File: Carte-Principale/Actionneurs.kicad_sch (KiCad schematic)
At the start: 0 parts

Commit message: Moteurs + Encodeurs
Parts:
- added U7: PCA9685PW, Package_SO:TSSOP-28_4.4x9.7mm_P0.65mm, symbol Driver_LED:PCA9685PW
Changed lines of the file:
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@@
 	(generator_version "8.0")
 	(paper "A4")
+	(symbol
+		(lib_id "Driver_LED:PCA9685PW")
+		(at 151.13 81.28 0)
+		(unit 1)
+		(exclude_from_sim no)
+		(in_bom yes)
+		(on_board yes)
+		(dnp no)
+		(fields_autoplaced yes)
+		(property "Reference" "U7"
+			(at 153.3241 55.88 0)
+			(effects
+				(font
+					(size 1.27 1.27)
+				)
+				(justify left)
+			)
+		)
+		(property "Value" "PCA9685PW"
+			(at 153.3241 58.42 0)
+			(effects
+				(font
+					(size 1.27 1.27)
+				)
+				(justify left)
+			)
+		)
+		(property "Footprint" "Package_SO:TSSOP-28_4.4x9.7mm_P0.65mm"
+			(at 151.765 106.045 0)
+			(effects
+				(font
+					(size 1.27 1.27)
+				)
+				(justify left)
+				(hide yes)
+			)
+		)
+		(property "Datasheet" "http://www.nxp.com/docs/en/data-sheet/PCA9685.pdf"
+			(at 140.97 63.5 0)
+			(effects
+				(font
+					(size 1.27 1.27)
+				)
+				(hide yes)
+			)
+		)
+		(property "Description" "16-channel 12-bit PWM Fm+ I2C-bus LED controller RGBA TSSOP"
+			(at 151.13 81.28 0)
+			(effects
+				(font
+					(size 1.27 1.27)
+				)
+				(hide yes)
+			)
+		)
+		(pin "20"
+		)
+		(pin "28"
+		)
+		(pin "16"
+		)
+		(pin "10"
+		)
+		(pin "15"
+		)
+		(pin "9"
+		)
+		(pin "27"
+		)
+		(pin "12"
+		)
+		(pin "2"
+		)
+		(pin "21"
+		)
+		(pin "22"
+		)
+		(pin "8"
+		)
+		(pin "17"
+		)
+		(pin "11"
+		)
+		(pin "3"
+		)
+		(pin "24"
+		)
+		(pin "5"
+		)
+		(pin "25"
+		)
+		(pin "6"
+		)
+		(pin "1"
+		)
+		(pin "14"
+		)
+		(pin "7"
+		)
+		(pin "23"
+		)
+		(pin "4"
+		)
+		(pin "18"
+		)
+		(pin "13"
+		)
+		(pin "19"
+		)
+		(pin "26"
+		)
+		(instances
+			(project "Carte-Principale"
+				(path "/88b0dd29-ac24-4c5d-804c-fc642ecf6263/ec3b2e47-1720-4ba3-b32d-adf5bc711683"
+					(reference "U7")
+					(unit 1)
+				)
+			)
+		)
+	)
 )

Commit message: Avancée Actionneur
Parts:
- added C5: 10u, symbol Device:C
- added C6: x, symbol Device:C_Polarized
- added D1: RGB_LED, symbol Device:LED_BGKR
- added J5: AX12, symbol Connector:Conn_01x03_Pin
- added JP1: A0, symbol Jumper:SolderJumper_2_Open
- added JP2: A1, symbol Jumper:SolderJumper_2_Open
- added JP3: A2, symbol Jumper:SolderJumper_2_Open
- added JP4: A3, symbol Jumper:SolderJumper_2_Open
- added JP5: A4, symbol Jumper:SolderJumper_2_Open
- added JP6: A5, symbol Jumper:SolderJumper_2_Open
- added M1, M10, M11, M12, M13, M2, M3, M4, M5, M6, M7, M8, M9: Motor_Servo, Connector_PinHeader_2.54mm:PinHeader_1x03_P2.54mm_Vertical, symbol Motor:Motor_Servo
- added R10, R11, R6, R7, R8, R9: 10k, symbol Device:R
- added R12, R13, R14, R15, R16, R17, R18, R19, R20, R21, R22, R23, R24, R25, R26, R27: 220, symbol Device:R
- added R5: 10k, symbol Device:R_Small
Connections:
- net at U7.1 (A0): now also JP1.2 (B), R11.1
- net at U7.10 (LED4): now also R16.1
- net at U7.11 (LED5): now also R17.1
- net at U7.12 (LED6): now also R18.1
- net at U7.13 (LED7): now also R19.1
- net GND: now reaches U7.14 (VSS)
- net GND: now also U7.25 (EXTCLK), C5.1, C6.2, D1.3 (K), M1.3 (-), M10.3 (-), M11.3 (-), M12.3 (-), M13.3 (-), M2.3 (-), M3.3 (-), M4.3 (-), M5.3 (-), M6.3 (-), M7.3 (-), M8.3 (-), M9.3 (-), R10.2, R11.2, R5.2, R6.2, R7.2, R8.2, R9.2
- net at U7.15 (LED8): now also R20.1
- net at U7.16 (LED9): now also R21.1
- net at U7.17 (LED10): now also R22.1
- net at U7.18 (LED11): now also R23.1
- net at U7.19 (LED12): now also R24.1
- net at U7.2 (A1): now also JP2.2 (B), R10.1
- net at U7.20 (LED13): now also R25.1
- net at U7.21 (LED14): now also R26.1
- net at U7.22 (LED15): now also R27.1
- net at U7.23 (~{OE}): now also R5.1
- net at U7.24 (A5): now also JP6.2 (B), R6.1
- net SCL: now reaches U7.26 (SCL)
- net SDA: now reaches U7.27 (SDA)
- net +5V: now reaches U7.28 (VDD)
- net +5V: now also C5.2, JP1.1 (A), JP2.1 (A), JP3.1 (A), JP4.1 (A), JP5.1 (A), JP6.1 (A)
- net at U7.3 (A2): now also JP3.2 (B), R9.1
- net at U7.4 (A3): now also JP4.2 (B), R8.1
- net at U7.5 (A4): now also JP5.2 (B), R7.1
- net at U7.6 (LED0): now also R13.1
- net at U7.7 (LED1): now also R12.1
- net at U7.8 (LED2): now also R14.1
- net at U7.9 (LED3): now also R15.1
- new net +5VA: C6.1, M1.2 (+), M10.2 (+), M11.2 (+), M12.2 (+), M13.2 (+), M2.2 (+), M3.2 (+), M4.2 (+), M5.2 (+), M6.2 (+), M7.2 (+), M8.2 (+), M9.2 (+)
- new net PWM0: M1.1 (PWM), R13.2
- new net PWM1: M2.1 (PWM), R12.2
- new net PWM10: M11.1 (PWM), R22.2
- new net PWM11: M12.1 (PWM), R23.2
- new net PWM12: M13.1 (PWM), R24.2
- new net PWM13: D1.1 (BA), R25.2
- new net PWM14: D1.2 (GA), R26.2
- new net PWM15: D1.4 (RA), R27.2
- new net PWM2: M3.1 (PWM), R14.2
- new net PWM3: M4.1 (PWM), R15.2
- new net PWM4: M5.1 (PWM), R16.2
- new net PWM5: M6.1 (PWM), R17.2
- new net PWM6: M7.1 (PWM), R18.2
- new net PWM7: M8.1 (PWM), R19.2
- new net PWM8: M9.1 (PWM), R20.2
- new net PWM9: M10.1 (PWM), R21.2

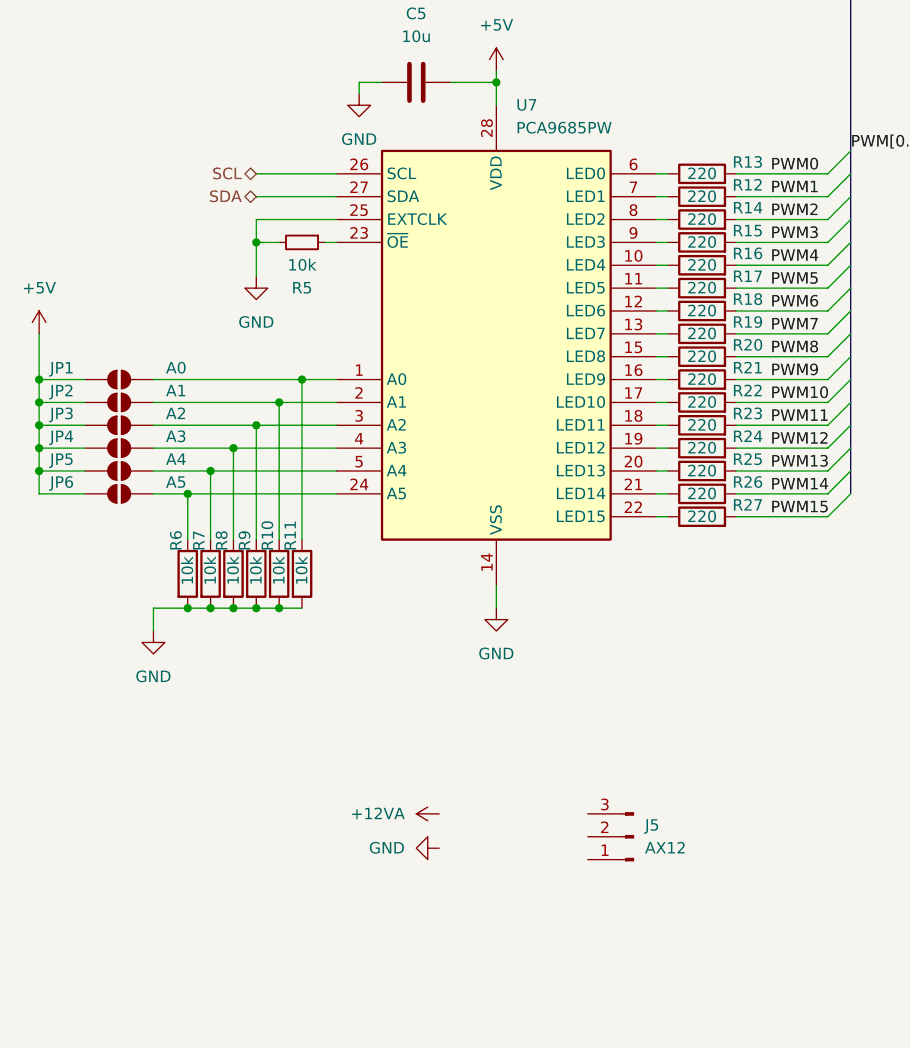
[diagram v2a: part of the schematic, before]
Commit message: Rajout écran
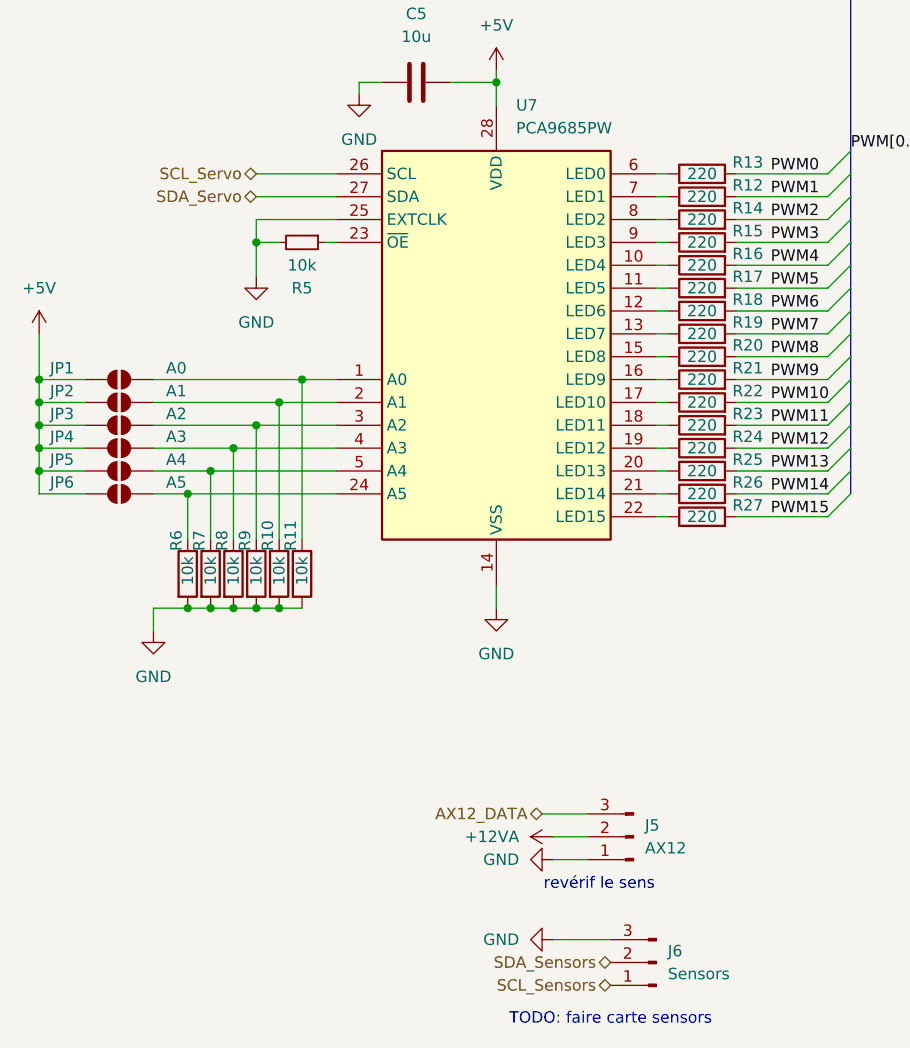
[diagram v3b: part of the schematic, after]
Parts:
- added J6: Sensors, symbol Connector:Conn_01x03_Pin
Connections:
- net +12VA: now also J5.2 (Pin_2)
- net GND: now also J5.1 (Pin_1), J6.3 (Pin_3)
- net AX12_DATA: now reaches J5.3 (Pin_3)
- net SCL renamed SCL_Servo
- net SDA renamed SDA_Servo
- new net SCL_Sensors: J6.1 (Pin_1)
- new net SDA_Sensors: J6.2 (Pin_2)
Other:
- note added: "TODO: faire carte sensors"
- note added: "revérif le sens"

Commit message: wiring
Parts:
- removed C5: 10u, symbol Device:C
- removed C6: x, symbol Device:C_Polarized
- removed D1: RGB_LED, symbol Device:LED_BGKR
- removed J6: Sensors, symbol Connector:Conn_01x03_Pin
- removed JP1: A0, symbol Jumper:SolderJumper_2_Open
- removed JP2: A1, symbol Jumper:SolderJumper_2_Open
- removed JP3: A2, symbol Jumper:SolderJumper_2_Open
- removed JP4: A3, symbol Jumper:SolderJumper_2_Open
- removed JP5: A4, symbol Jumper:SolderJumper_2_Open
- removed JP6: A5, symbol Jumper:SolderJumper_2_Open
- removed M1, M10, M11, M12, M13, M2, M3, M4, M5, M6, M7, M8, M9: Motor_Servo, Connector_PinHeader_2.54mm:PinHeader_1x03_P2.54mm_Vertical, symbol Motor:Motor_Servo
- removed R10, R11, R6, R7, R8, R9: 10k, symbol Device:R
- removed R12, R13, R14, R15, R16, R17, R18, R19, R20, R21, R22, R23, R24, R25, R26, R27: 220, symbol Device:R
- removed R5: 10k, symbol Device:R_Small
- removed U7: PCA9685PW, Package_SO:TSSOP-28_4.4x9.7mm_P0.65mm, symbol Driver_LED:PCA9685PW
- added J10: I2C_Sensors, Connector_PinSocket_2.54mm:PinSocket_1x04_P2.54mm_Vertical, symbol Connector:Conn_01x04_Pin
- added J8: PCA9685, Connector_PinSocket_2.54mm:PinSocket_1x03_P2.54mm_Vertical, symbol Connector:Conn_01x03_Pin
- J9: renamed from J5; footprint (none) -> Connector_PinSocket_2.54mm:PinSocket_1x03_P2.54mm_Vertical
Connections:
- net GND: now also J10.1 (Pin_1), J8.1 (Pin_1)
- net SCL_Sensors: now also J10.2 (Pin_2)
- net SCL_Servo: now also J8.2 (Pin_2)
- net SDA_Sensors: now also J10.3 (Pin_3)
- net SDA_Servo: now also J8.3 (Pin_3)
- new net IT_Ready_Sensors: J10.4 (Pin_4)
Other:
- note added: "On peut acheter le PCB pour les Servos https://www.adafruit.com/product/815"
- moved on the sheet: J9

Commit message: Schéma vérifié
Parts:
- removed J8: PCA9685, Connector_PinSocket_2.54mm:PinSocket_1x03_P2.54mm_Vertical, symbol Connector:Conn_01x03_Pin
- added J15: PCA9685, Connector_Molex:Molex_KK-254_AE-6410-06A_1x06_P2.54mm_Vertical, symbol Connector:Conn_01x06_Pin
- J16: renamed from J9; footprint Connector_PinSocket_2.54mm:PinSocket_1x03_P2.54mm_Vertical -> Connector_Molex:Molex_KK-254_AE-6410-03A_1x03_P2.54mm_Vertical
- J17: renamed from J10; footprint Connector_PinSocket_2.54mm:PinSocket_1x04_P2.54mm_Vertical -> Connector_Molex:Molex_KK-254_AE-6410-04A_1x04_P2.54mm_Vertical
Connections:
- net GND: now also J15.6 (Pin_6)
- net SCL_Servo: now also J15.4 (Pin_4)
- net SDA_Servo: now also J15.3 (Pin_3)
- new net +5V: J15.2 (Pin_2)
- new net +5VA: J15.1 (Pin_1)
- no-connect marks 0 -> 1
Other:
- note added: "TODO: faire carte sensors (bien penser aux R de termination)"
- note removed: "TODO: faire carte sensors"
- note removed: "revérif le sens"
- company: (none) -> CRINSA
- title: (none) -> Carte Principale
- moved on the sheet: J16, J17

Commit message: Avancée PCB
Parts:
- removed J15: PCA9685, Connector_Molex:Molex_KK-254_AE-6410-06A_1x06_P2.54mm_Vertical, symbol Connector:Conn_01x06_Pin
- added C5: 10u, Capacitor_SMD:C_1210_3225Metric_Pad1.33x2.70mm_HandSolder, symbol Device:C
- added C6: x, Capacitor_THT:CP_Radial_D8.0mm_P3.50mm, symbol Device:C_Polarized
- added D5, D6, D7: LED, LED_SMD:LED_2010_5025Metric_Pad1.52x2.65mm_HandSolder, symbol Device:LED
- added M1, M10, M11, M12, M13, M2, M3, M4, M5, M6, M7, M8, M9: Motor_Servo, Connector_PinHeader_2.54mm:PinHeader_1x03_P2.54mm_Vertical, symbol Motor:Motor_Servo
- added R10, R11, R12, R14, R15, R16, R17, R18, R19, R20, R21, R22, R23: 220, LED_SMD:LED_1210_3225Metric_Pad1.42x2.65mm_HandSolder, symbol Device:R
- added R13: 10k, LED_SMD:LED_1210_3225Metric_Pad1.42x2.65mm_HandSolder, symbol Device:R_Small
- added R24, R25, R26: x, LED_SMD:LED_1210_3225Metric_Pad1.42x2.65mm_HandSolder, symbol Device:R
- added U7: PCA9685PW, Package_SO:TSSOP-28_4.4x9.7mm_P0.65mm, symbol Driver_LED:PCA9685PW
- renumbered J16 to J12, J17 to J13
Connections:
- net +5V: now also C5.2, U7.1 (A0), U7.28 (VDD)
- net +5VA: now also C6.1, M1.2 (+), M10.2 (+), M11.2 (+), M12.2 (+), M13.2 (+), M2.2 (+), M3.2 (+), M4.2 (+), M5.2 (+), M6.2 (+), M7.2 (+), M8.2 (+), M9.2 (+)
- net GND: now also C5.1, C6.2, D5.1 (K), D6.1 (K), D7.1 (K), M1.3 (-), M10.3 (-), M11.3 (-), M12.3 (-), M13.3 (-), M2.3 (-), M3.3 (-), M4.3 (-), M5.3 (-), M6.3 (-), M7.3 (-), M8.3 (-), M9.3 (-), R13.2, U7.14 (VSS), U7.2 (A1), U7.24 (A5), U7.25 (EXTCLK), U7.3 (A2), U7.4 (A3), U7.5 (A4)
- net SCL_Servo: now also U7.26 (SCL)
- net SDA_Servo: now also U7.27 (SDA)
- new net: R11.1, U7.7 (LED1)
- new net: R25.1, U7.21 (LED14)
- new net: R14.1, U7.9 (LED3)
- new net: R21.1, U7.17 (LED10)
- new net: R19.1, U7.15 (LED8)
- new net: R23.1, U7.19 (LED12)
- new net: R26.1, U7.22 (LED15)
- new net: R24.1, U7.20 (LED13)
- new net: R15.1, U7.10 (LED4)
- new net: R22.1, U7.18 (LED11)
- new net: R20.1, U7.16 (LED9)
- new net: R10.1, U7.6 (LED0)
- new net: R12.1, U7.8 (LED2)
- new net: R16.1, U7.11 (LED5)
- new net: R17.1, U7.12 (LED6)
- new net: R18.1, U7.13 (LED7)
- new net: R13.1, U7.23 (~{OE})
- new net PWM0: M1.1 (PWM), R10.2
- new net PWM1: M3.1 (PWM), R11.2
- new net PWM10: M6.1 (PWM), R21.2
- new net PWM11: M8.1 (PWM), R22.2
- new net PWM12: M10.1 (PWM), R23.2
- new net PWM13: D5.2 (A), R24.2
- new net PWM14: D6.2 (A), R25.2
- new net PWM15: D7.2 (A), R26.2
- new net PWM2: M5.1 (PWM), R12.2
- new net PWM3: M7.1 (PWM), R14.2
- new net PWM4: M9.1 (PWM), R15.2
- new net PWM5: M11.1 (PWM), R16.2
- new net PWM6: M12.1 (PWM), R17.2
- new net PWM7: M13.1 (PWM), R18.2
- new net PWM8: M2.1 (PWM), R19.2
- new net PWM9: M4.1 (PWM), R20.2
- no-connect marks 1 -> 0
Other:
- note added: "Adresse: 1000 001x"
- moved on the sheet: J12, J13

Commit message: avancée
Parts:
- R16: renamed from R19; footprint LED_SMD:LED_1210_3225Metric_Pad1.42x2.65mm_HandSolder -> Resistor_SMD:R_1210_3225Metric_Pad1.30x2.65mm_HandSolder
- R18: renamed from R17; footprint LED_SMD:LED_1210_3225Metric_Pad1.42x2.65mm_HandSolder -> Resistor_SMD:R_1210_3225Metric_Pad1.30x2.65mm_HandSolder
- R19: renamed from R16; footprint LED_SMD:LED_1210_3225Metric_Pad1.42x2.65mm_HandSolder -> Resistor_SMD:R_1210_3225Metric_Pad1.30x2.65mm_HandSolder
- R2: renamed from R24; footprint LED_SMD:LED_1210_3225Metric_Pad1.42x2.65mm_HandSolder -> Resistor_SMD:R_1210_3225Metric_Pad1.30x2.65mm_HandSolder
- R20: renamed from R18; footprint LED_SMD:LED_1210_3225Metric_Pad1.42x2.65mm_HandSolder -> Resistor_SMD:R_1210_3225Metric_Pad1.30x2.65mm_HandSolder
- R22: renamed from R15; footprint LED_SMD:LED_1210_3225Metric_Pad1.42x2.65mm_HandSolder -> Resistor_SMD:R_1210_3225Metric_Pad1.30x2.65mm_HandSolder
- R23: footprint LED_SMD:LED_1210_3225Metric_Pad1.42x2.65mm_HandSolder -> Resistor_SMD:R_1210_3225Metric_Pad1.30x2.65mm_HandSolder
- R24: renamed from R22; footprint LED_SMD:LED_1210_3225Metric_Pad1.42x2.65mm_HandSolder -> Resistor_SMD:R_1210_3225Metric_Pad1.30x2.65mm_HandSolder
- R25: renamed from R20; footprint LED_SMD:LED_1210_3225Metric_Pad1.42x2.65mm_HandSolder -> Resistor_SMD:R_1210_3225Metric_Pad1.30x2.65mm_HandSolder
- R26: renamed from R21; footprint LED_SMD:LED_1210_3225Metric_Pad1.42x2.65mm_HandSolder -> Resistor_SMD:R_1210_3225Metric_Pad1.30x2.65mm_HandSolder
- R5: renamed from R25; footprint LED_SMD:LED_1210_3225Metric_Pad1.42x2.65mm_HandSolder -> Resistor_SMD:R_1210_3225Metric_Pad1.30x2.65mm_HandSolder
- R6: renamed from R26; footprint LED_SMD:LED_1210_3225Metric_Pad1.42x2.65mm_HandSolder -> Resistor_SMD:R_1210_3225Metric_Pad1.30x2.65mm_HandSolder
- renumbered C6 to C1, C5 to C2, D7 to D1, D5 to D2, D6 to D3, J13 to J17, J12 to J20, M2 to M10, M8 to M11, M11 to M13, M7 to M2, M5 to M4, M9 to M5, M4 to M6, M13 to M7, M10 to M8, M6 to M9, R12 to R13, R10 to R14, R11 to R15, R14 to R17, R13 to R21, U7 to U1
